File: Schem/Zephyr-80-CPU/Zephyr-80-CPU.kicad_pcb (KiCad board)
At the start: 6 copper layers, 160 x 64.4 mm, 22 parts, among them J1 pBITzBus, U1 AS7C4096A-12TCN, U2 ATF22V10C-10PU, U3 Z084000xP, U4 SST39SF040-70-4C-PHE, U5 ATF22V10C-10PU, U6 SN74HC273DWR, U7 SN74HC244DWR, Y1 ECS-2100AX-100

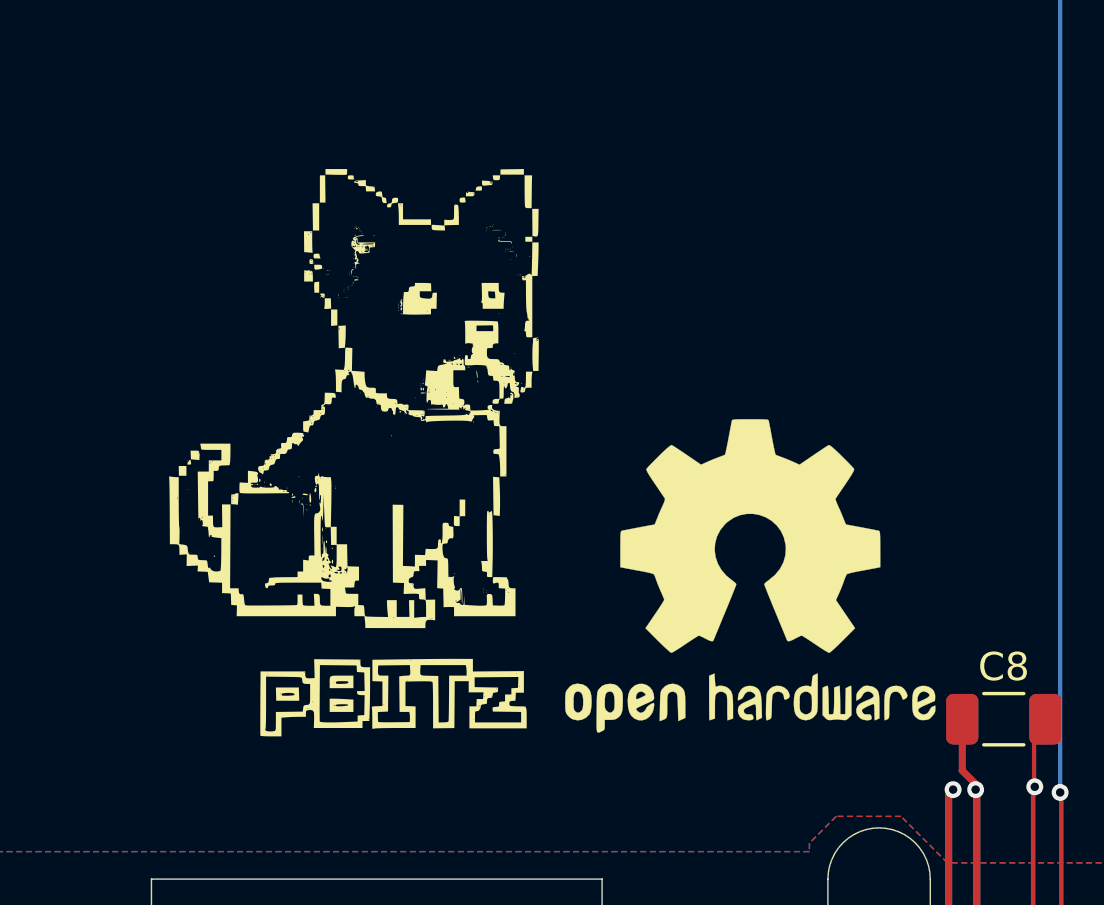
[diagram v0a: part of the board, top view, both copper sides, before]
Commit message: Added Zephyr-80 Logo
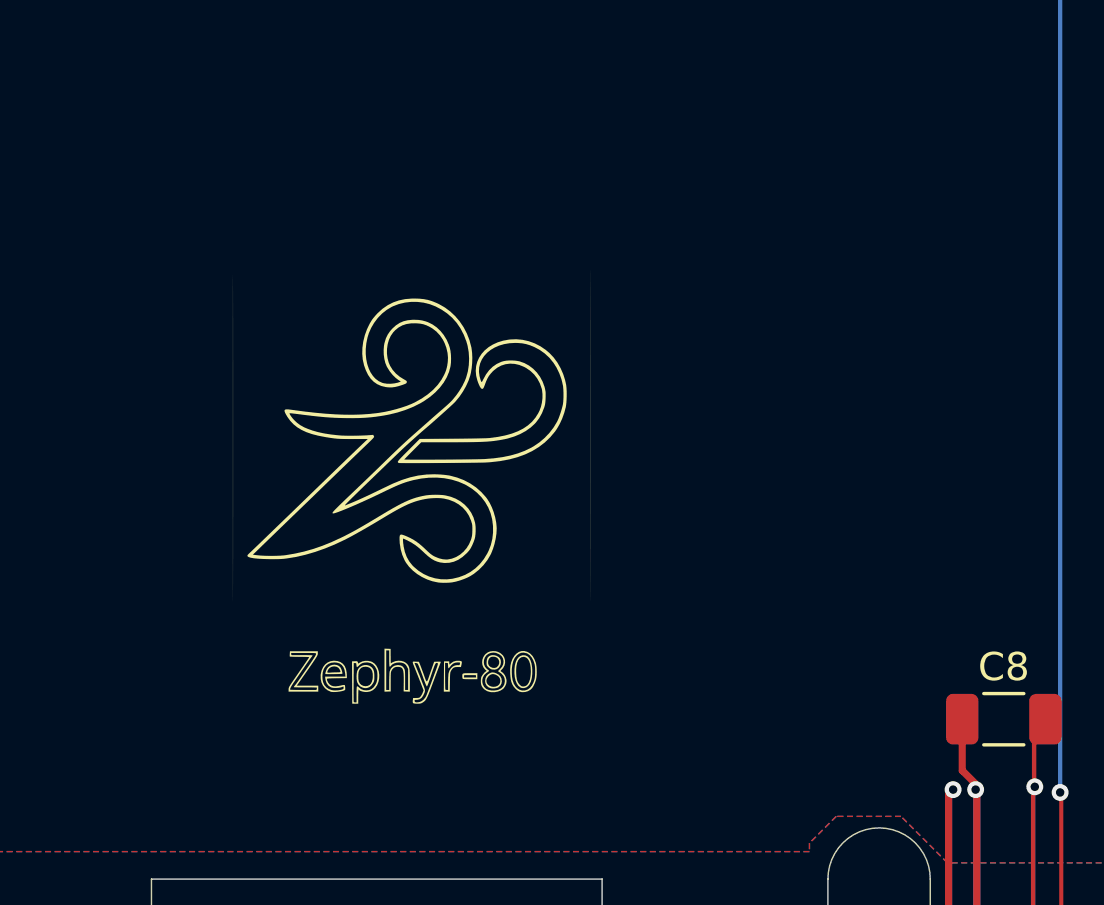
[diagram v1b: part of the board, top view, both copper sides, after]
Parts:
- added G***: LOGO, Footprints:zephir-80-Silk, F.Cu at (108.9, 91.6)
- G***, REF**: moved to B.Cu
- moved REF** 14.3 mm to (106.6, 96.6), turned to 180 degrees
- moved G*** 11.0 mm to (119.2, 90.9), turned to 180 degrees
